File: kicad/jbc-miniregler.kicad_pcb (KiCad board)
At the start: 2 copper layers, 110 x 100 mm, 168 parts, among them J1 Makita Plus, J10 Makita Minus, J12 ActivEnergy B2-, J13 ActivEnergy B1-, J2 Makita Minus, J4 USB_B, J5 AVR ISP, J6 ActivEnergy B2+, J7 ActivEnergy B1+, J8 Makita Plus, Q1 KND3508A, Q2 2N7002, Q3 MMBT3904, Q4 MMBT3904, Q5 ZXMP10A13FTA, SW1 UP, SW2 DOWN, SW3 ENTER, SW4 BACK, SW5 Reset, SW6 Ein/Aus, U1 OLED-128x32-Module, U10 MAX3232, U11 YD3082EESA, U2 74LVC1G125, U3 NST175, U4 CH340C, U5 ATmega328P-AU, U6 GS8332-SR, U7 PN7006A, U8 XL7005A, U9 XL7005A, X1 POWER, X2 COM, X3 Lötkolben, Y1 16MHz

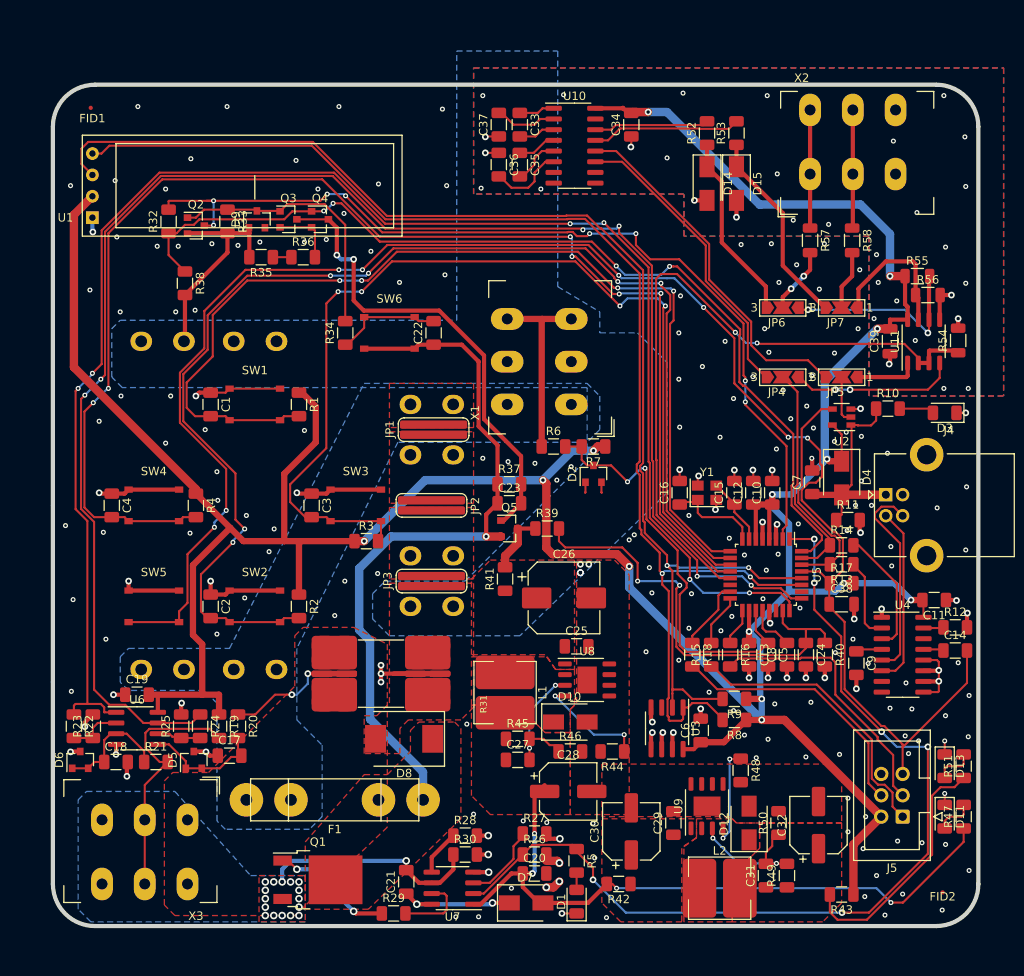
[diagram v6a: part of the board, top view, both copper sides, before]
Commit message: Layout Fertig, TODOs: Beschriftungen fertig stellen, ...
RS485 TVS-Diode
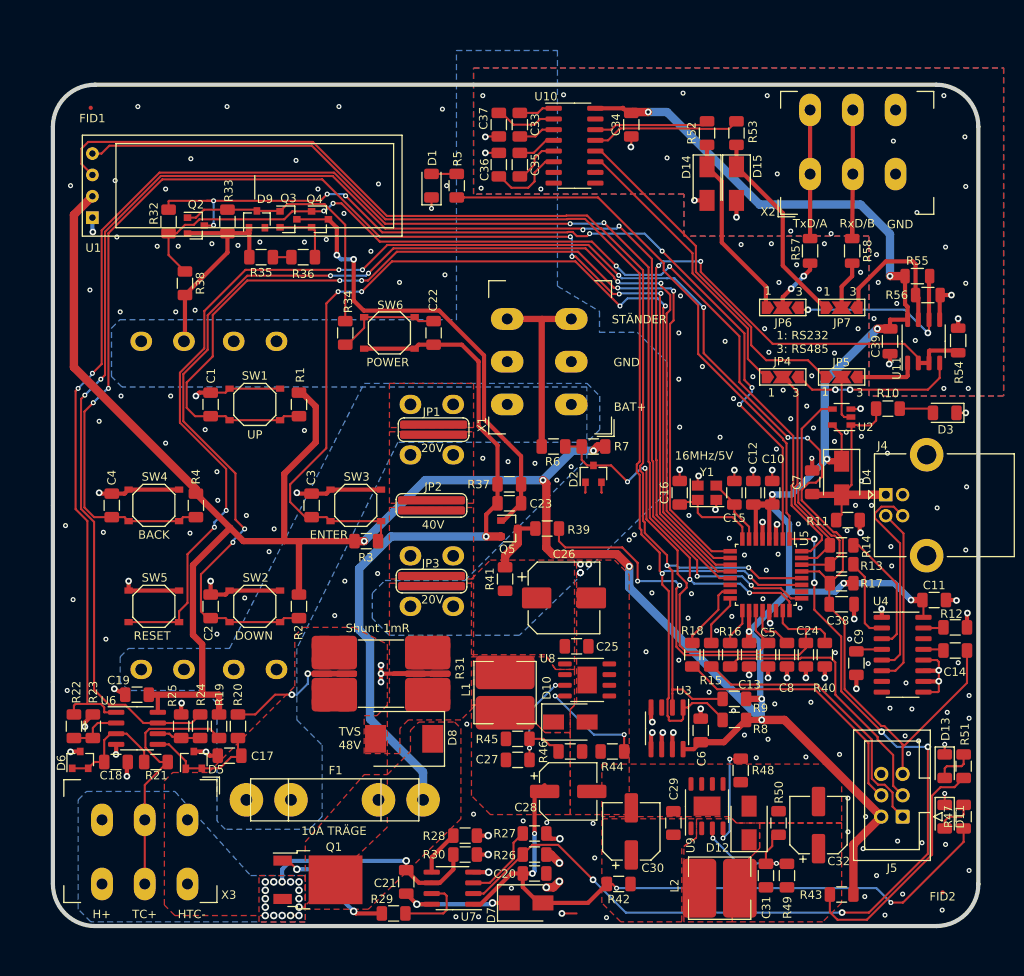
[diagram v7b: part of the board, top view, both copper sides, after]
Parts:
- moved D1 86.8 mm to (136.0, 55.0)
- moved R5 81.5 mm to (139.0, 55.0), turned to 90 degrees
- moved R57 1.25 mm to (181.0, 62.8)
- moved R58 1.25 mm to (186.0, 62.8)
- turned JP4 to 0 degrees
- turned JP5 to 0 degrees
- turned JP6 to 0 degrees
- turned JP7 to 0 degrees
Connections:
- net Net-(R52-Pad2) renamed /UART RS232/RS485/Tx
- net Net-(R53-Pad2) renamed /UART RS232/RS485/Rx
- D14 pad 1: Net-(D14-Pad1) -> /UART RS232/RS485/TxD
- D15 pad 1: Net-(D15-Pad1) -> /UART RS232/RS485/RxD
- JP4 pad : (no net) -> /UART RS232/RS485/di
- JP4 pad 1: Net-(JP4-Pad1) -> /UART RS232/RS485/tin
- JP4 pad 3: Net-(JP4-Pad3) -> /UART RS232/RS485/di
- JP5 pad : (no net) -> /UART RS232/RS485/ro
- JP5 pad 1: Net-(JP5-Pad1) -> /UART RS232/RS485/rout
- JP5 pad 3: Net-(JP5-Pad3) -> /UART RS232/RS485/ro
- JP6 pad : (no net) -> /UART RS232/RS485/A
- JP6 pad 1: Net-(JP6-Pad1) -> /UART RS232/RS485/TxD
- JP6 pad 3: Net-(D14-Pad1) -> /UART RS232/RS485/A
- JP7 pad 1: Net-(JP7-Pad1) -> /UART RS232/RS485/RxD
- JP7 pad 3: Net-(D15-Pad1) -> /UART RS232/RS485/B
- R52 pad 1: Net-(D14-Pad1) -> /UART RS232/RS485/TxD
- R53 pad 1: Net-(D15-Pad1) -> /UART RS232/RS485/RxD
- R55 pad 2: Net-(JP6-Pad1) -> /UART RS232/RS485/A
- R56 pad 1: Net-(JP7-Pad1) -> /UART RS232/RS485/B
- U10 pad 11: Net-(JP4-Pad3) -> /UART RS232/RS485/tin
- U10 pad 12: Net-(JP5-Pad3) -> /UART RS232/RS485/rout
- U11 pad 1: Net-(JP5-Pad1) -> /UART RS232/RS485/ro
- U11 pad 4: Net-(JP4-Pad1) -> /UART RS232/RS485/di
- U11 pad 6: Net-(JP6-Pad1) -> /UART RS232/RS485/A
- U11 pad 7: Net-(JP7-Pad1) -> /UART RS232/RS485/B
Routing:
- net /Arduino/Heizelement: track 112.0 -> 177.6 mm
- net Net-(JP5-Pad3): track 42.5 -> 0.00 mm
- net /UART RS232/RS485/rout: track 0.00 -> 41.5 mm
- net Net-(JP4-Pad3): track 35.9 -> 0.00 mm
- net /UART RS232/RS485/tin: track 0.00 -> 34.4 mm
- net Net-(D15-Pad1): track 23.7 -> 0.00 mm
- net /UART RS232/RS485/RxD: track 0.00 -> 23.7 mm
- net Net-(JP6-Pad1): track 23.3 -> 0.00 mm, vias 2 -> 0
- net /UART RS232/RS485/A: track 0.00 -> 23.3 mm, vias 0 -> 2
- net Net-(D14-Pad1): track 22.2 -> 0.00 mm
- net /UART RS232/RS485/TxD: track 0.00 -> 22.2 mm
- net Net-(JP4-Pad1): track 19.6 -> 0.00 mm, vias 2 -> 0
- net /UART RS232/RS485/di: track 0.00 -> 19.6 mm, vias 0 -> 2
- net Net-(JP7-Pad1): track 17.2 -> 0.00 mm
- net /UART RS232/RS485/B: track 0.00 -> 17.2 mm
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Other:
- board text added: "10A TRÄGE"
- board text added: "16MHz/5V"
- board text added: "1: RS232 3: RS485"
- board text added: "20V"
- board text added: "40V"
- board text added: "BACK"
- board text added: "BAT+"
- board text added: "DOWN"
- board text added: "ENTER"
- board text added: "GND"
- board text added: "H+"
- board text added: "HTC-"
- board text added: "POWER"
- board text added: "RESET"
- board text added: "RxD/B"
- board text added: "STÄNDER"
- board text added: "Shunt 1mR"
- board text added: "TC+"
- board text added: "TVS 48V"
- board text added: "TxD/A"
- board text added: "UP"

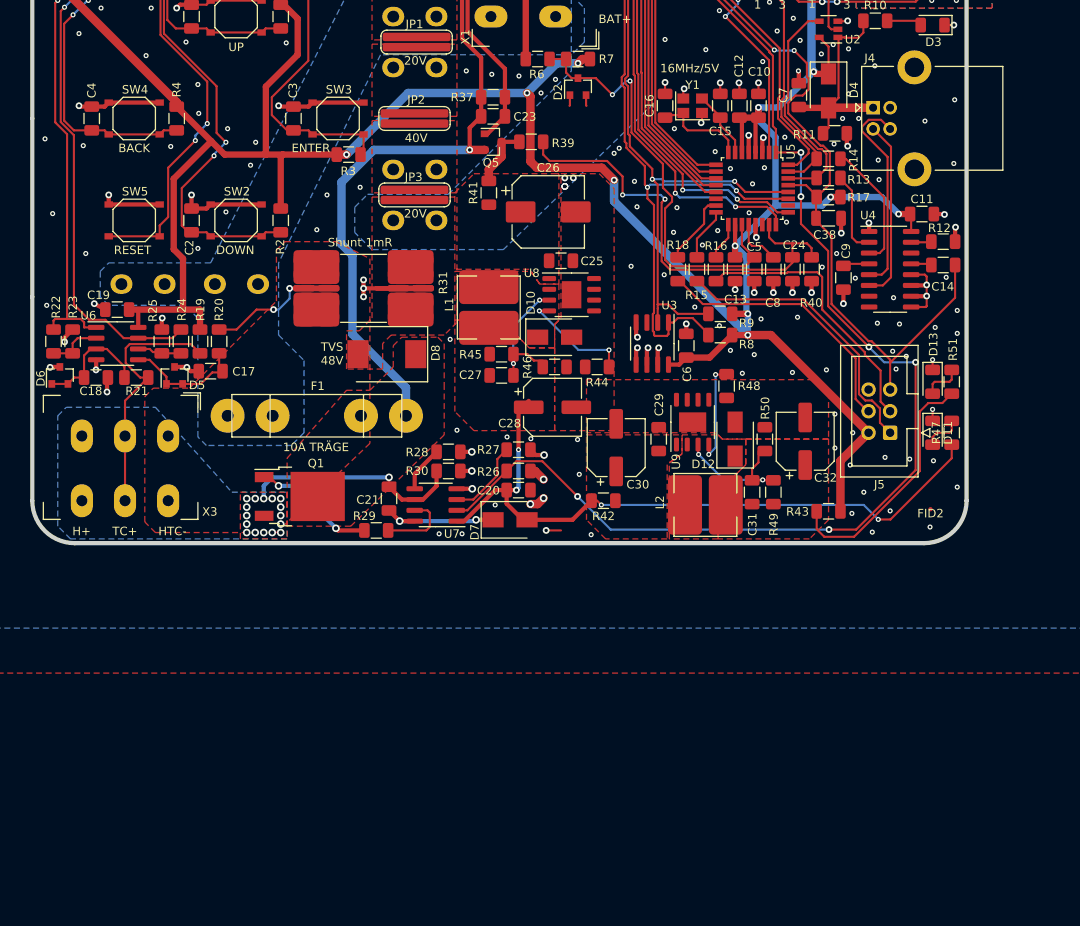
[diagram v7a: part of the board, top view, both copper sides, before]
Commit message: vor "update all footprints", FP-Lib Version V5.10
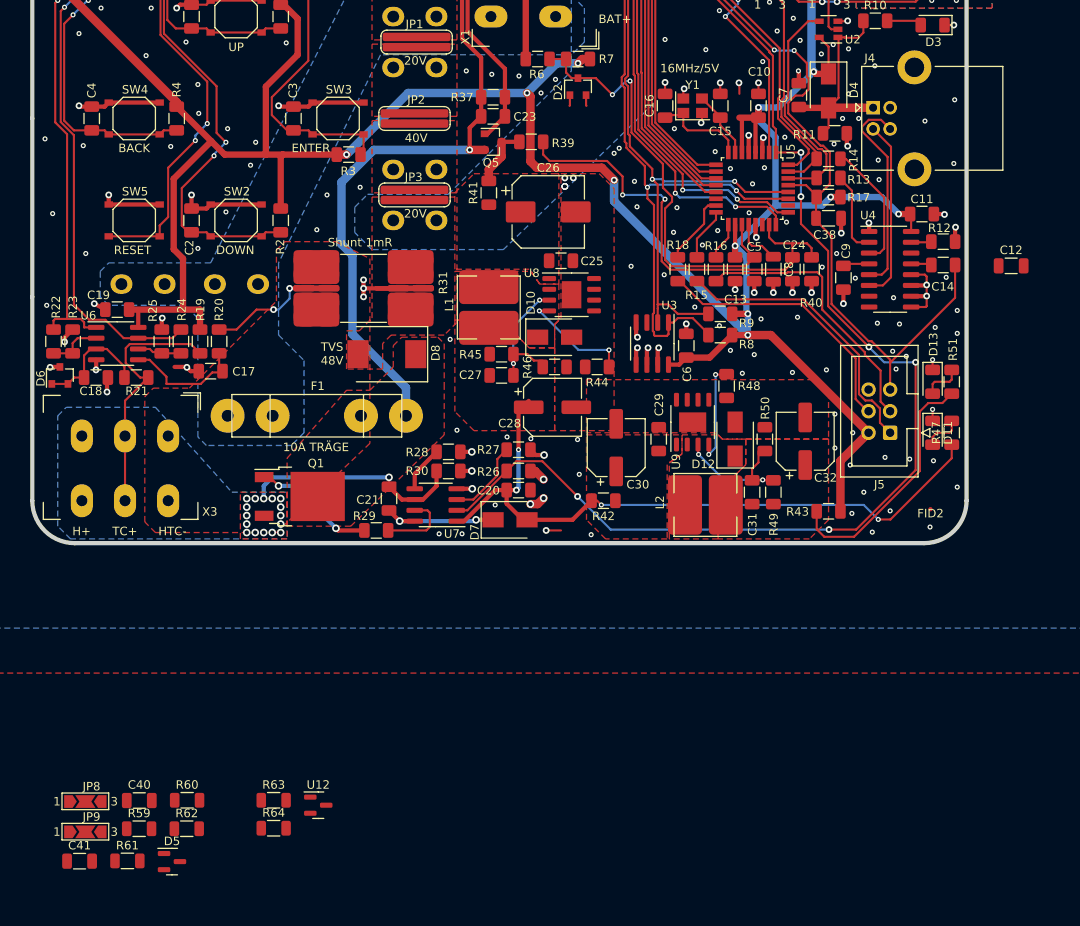
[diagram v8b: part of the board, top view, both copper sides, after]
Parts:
- added C40: 10n, Capacitor_SMD:C_1206_3216Metric, F.Cu at (103.6, 173.3)
- added C41: 10n, Capacitor_SMD:C_1206_3216Metric, F.Cu at (96.6, 180.4)
- added JP8: OP-Polarität, Jumper:SolderJumper-3_P2.0mm_Open_TrianglePad1.0x1.5mm_NumberLabels, F.Cu at (97.2, 173.4)
- added JP9: OP-Polarität, Jumper:SolderJumper-3_P2.0mm_Open_TrianglePad1.0x1.5mm_NumberLabels, F.Cu at (97.2, 177.0)
- added R59: 100R, Resistor_SMD:R_1206_3216Metric, F.Cu at (103.6, 176.6)
- added R60: 100R, Resistor_SMD:R_1206_3216Metric, F.Cu at (109.2, 173.3)
- added R61: 100R, Resistor_SMD:R_1206_3216Metric, F.Cu at (102.2, 180.4)
- added R62: 100R, Resistor_SMD:R_1206_3216Metric, F.Cu at (109.2, 176.6)
- added R63: 1k, Resistor_SMD:R_1206_3216Metric, F.Cu at (119.4, 173.3)
- added R64: 1k, Resistor_SMD:R_1206_3216Metric, F.Cu at (119.4, 176.6)
- added U12: TL431DBZ, Package_TO_SOT_SMD:SOT-23, F.Cu at (124.7, 173.8)
- C12: value 1u -> 100n
- C8: value 100n -> 1u
- moved D5 57.2 mm to (107.5, 180.5), turned to 0 degrees
- moved C12 37.1 mm to (206.2, 110.3), turned to 0 degrees
- turned C8 to 270 degrees
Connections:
- C12 pad 1: +5V -> GND
- C12 pad 2: GND -> +5V
- C8 pad 1: GND -> /Arduino/Arduino Nano/AREF
- C8 pad 2: /Arduino/Arduino Nano/AREF -> GND
- JP4 pad : /UART RS232/RS485/di -> (no net)
- JP5 pad : /UART RS232/RS485/ro -> (no net)
- JP6 pad : /UART RS232/RS485/A -> (no net)
- R22 pad 1: /Arduino/Temperatur -> Net-(R22-Pad1)
- R23 pad 2: GND -> Net-(JP9-Pad2)
- R24 pad 1: /Arduino/Strom -> Net-(R24-Pad1)
- U6 pad 1: /Arduino/Temperatur -> Net-(R22-Pad1)
- U6 pad 3: Net-(C18-Pad1) -> Net-(JP8-Pad2)
- U6 pad 5: Net-(C17-Pad2) -> Net-(R60-Pad2)
- U6 pad 7: /Arduino/Strom -> Net-(R24-Pad1)
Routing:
- net GND: track 143.4 -> 141.6 mm, vias 214 -> 213
- net Net-(JP9-Pad2): track 0.00 -> 1.84 mm, vias 0 -> 1
